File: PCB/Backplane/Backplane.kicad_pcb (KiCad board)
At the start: 4 copper layers, 40 x 100 mm, 79 parts, among them J1 ICSP, J2 Front, J3 Rear, J4 Bus In, J5 Bus Out, J6 Power In, J7 Power Out, Q1 Q_NMOS_GSD, Q2 Q_NMOS_GSD, SW1 Boot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

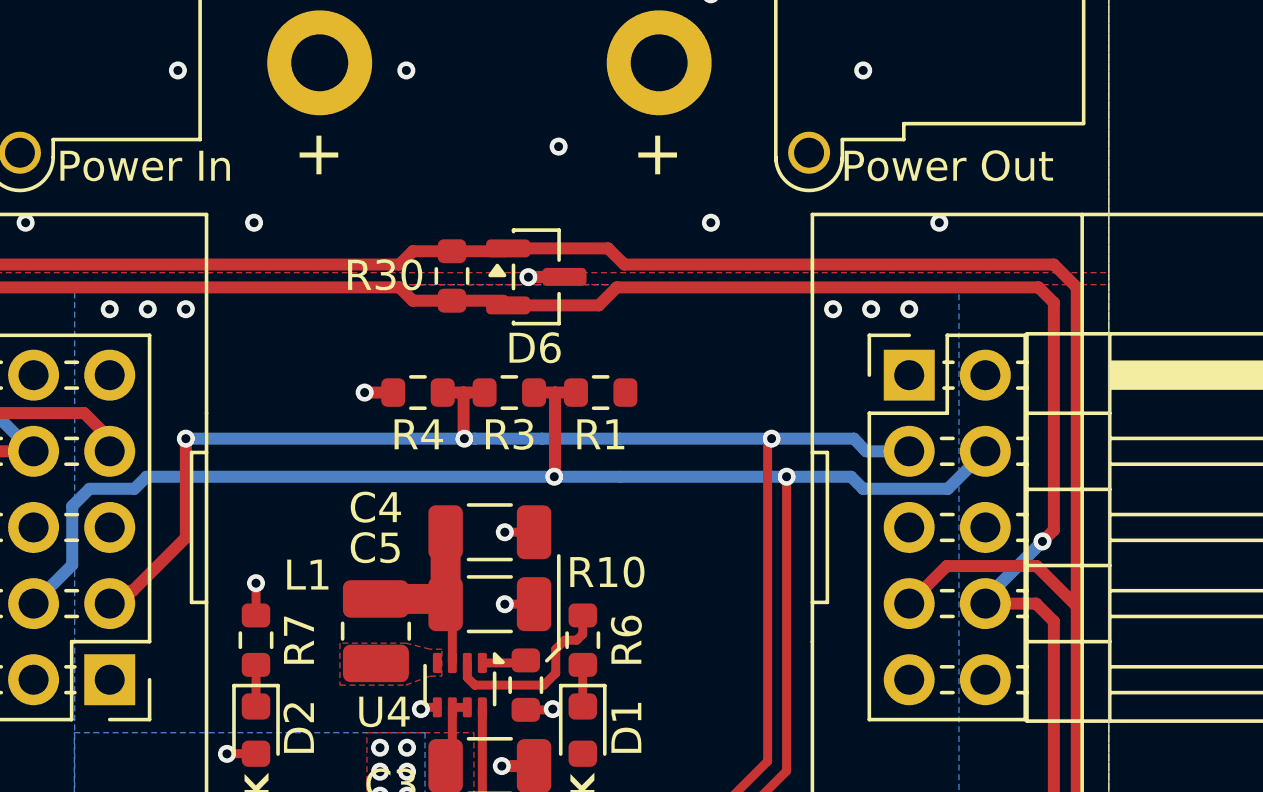
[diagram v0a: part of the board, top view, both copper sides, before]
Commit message: Add ESD protection to the RS485 networks.
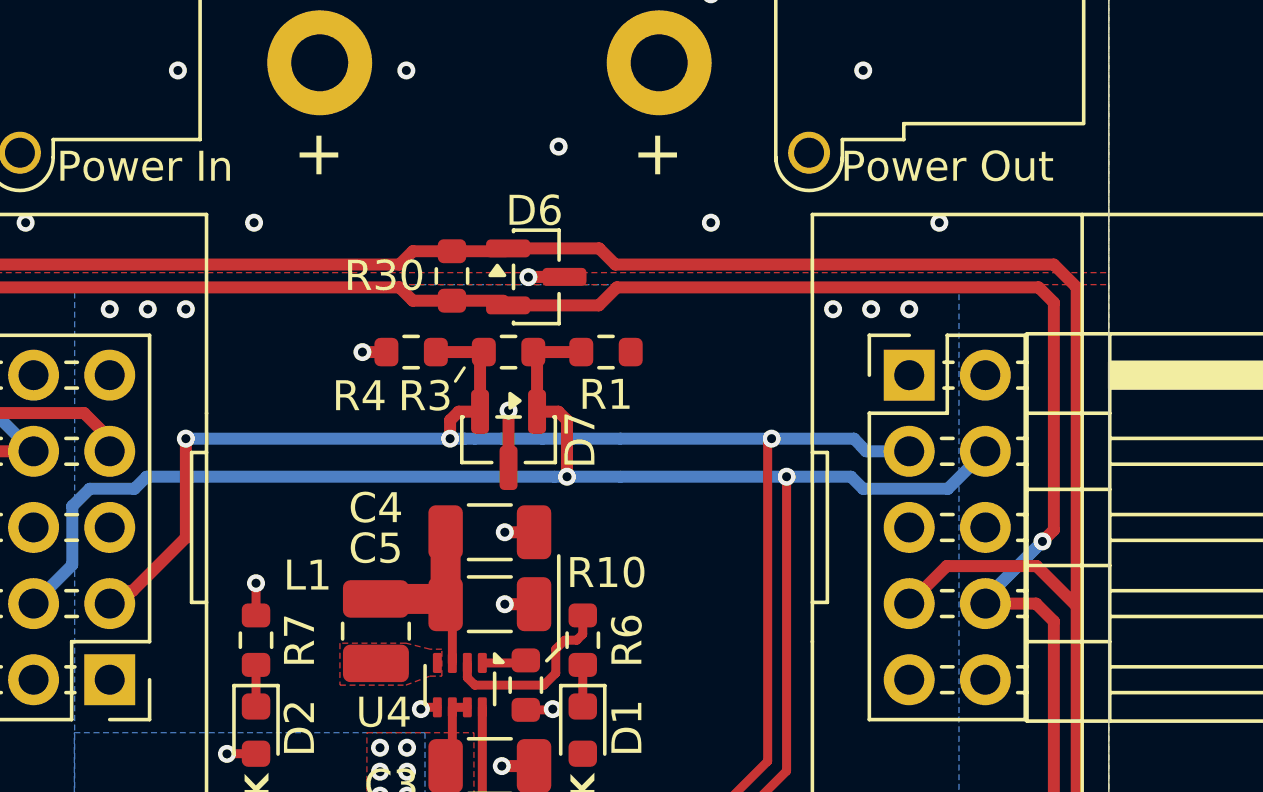
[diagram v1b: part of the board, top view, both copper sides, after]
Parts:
- added D7: T24CAN, Package_TO_SOT_SMD:SOT-23, F.Cu at (40.0, 50.1)
- moved R4 1.37 mm to (36.7, 47.1)
- moved R1 1.36 mm to (43.2, 47.1)
- moved R3 1.35 mm to (40.0, 47.1)
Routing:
- net A: track 60.9 -> 63.3 mm
- net B: track 56.2 -> 58.6 mm
- net GND: track 63.8 -> 65.6 mm, vias 51 -> 52

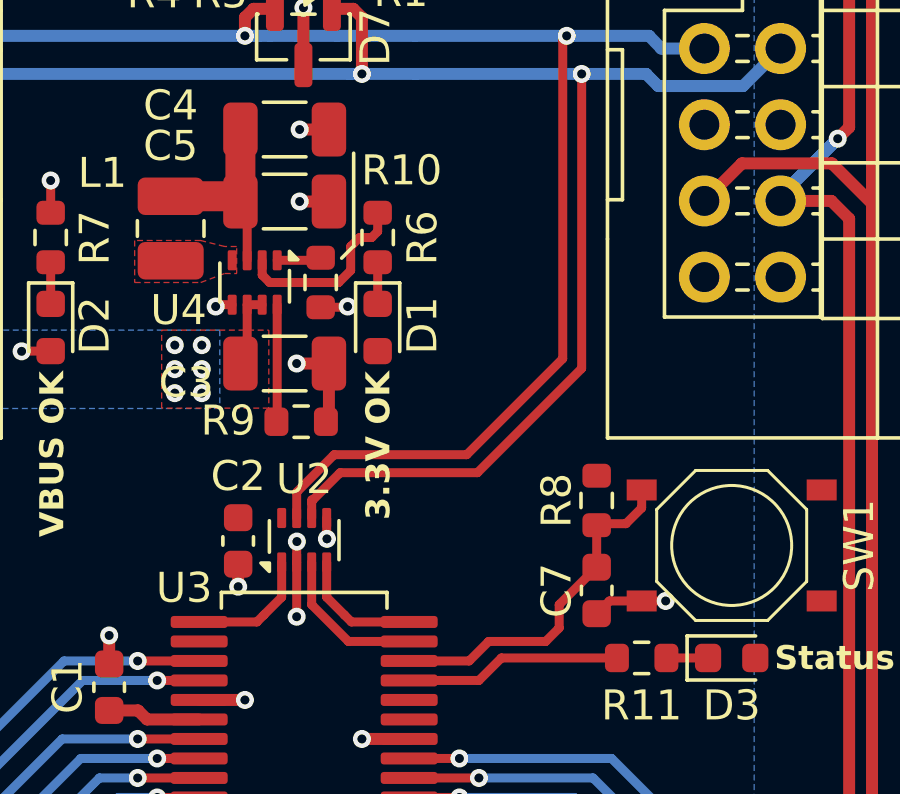
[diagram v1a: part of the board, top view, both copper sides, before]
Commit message: Fix up power LEDs on regulators.
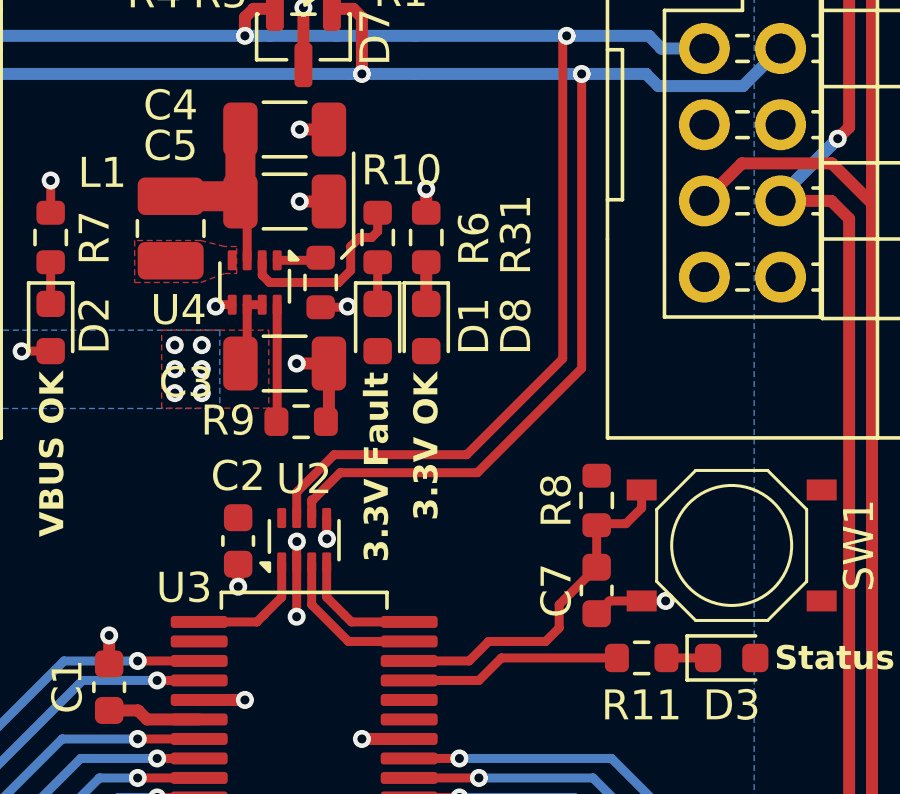
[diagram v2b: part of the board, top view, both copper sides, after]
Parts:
- added D8: 3.3V OK, LED_SMD:LED_0603_1608Metric, F.Cu at (44.1, 59.8)
- added R31: 10k, Resistor_SMD:R_0603_1608Metric, F.Cu at (44.1, 56.8)
- D1: value 3.3V OK -> 3.3V Fault
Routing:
- net Net-(D8-K): track 0.00 -> 1.39 mm
- net GND: track 65.6 -> 66.4 mm, vias 52 -> 53
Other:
- board text added: "3.3V Fault"

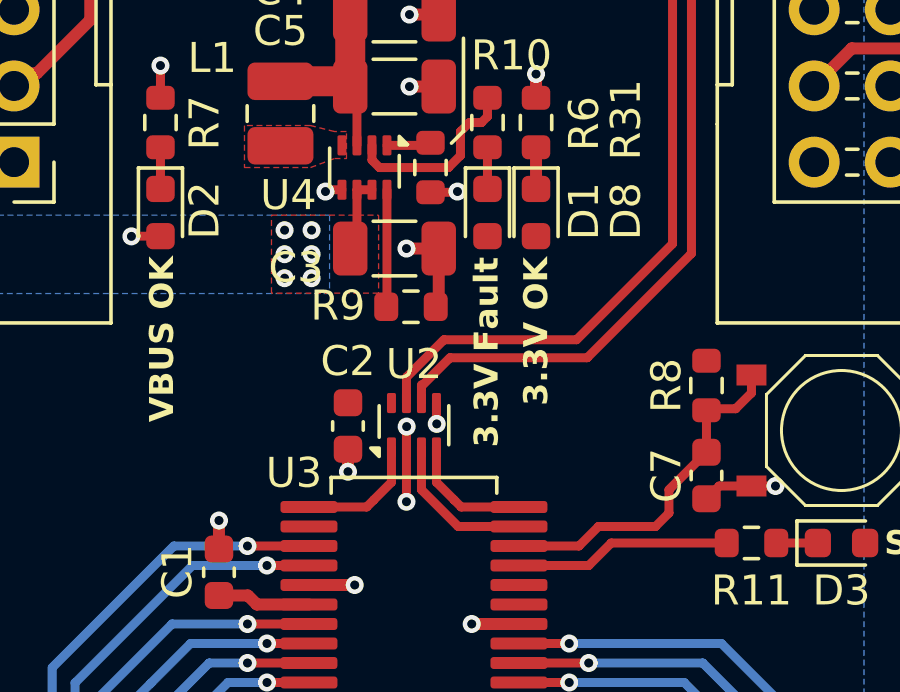
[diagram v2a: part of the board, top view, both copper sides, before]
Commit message: Include all corrections, mint new gerbers. Update some to KiCad 10.
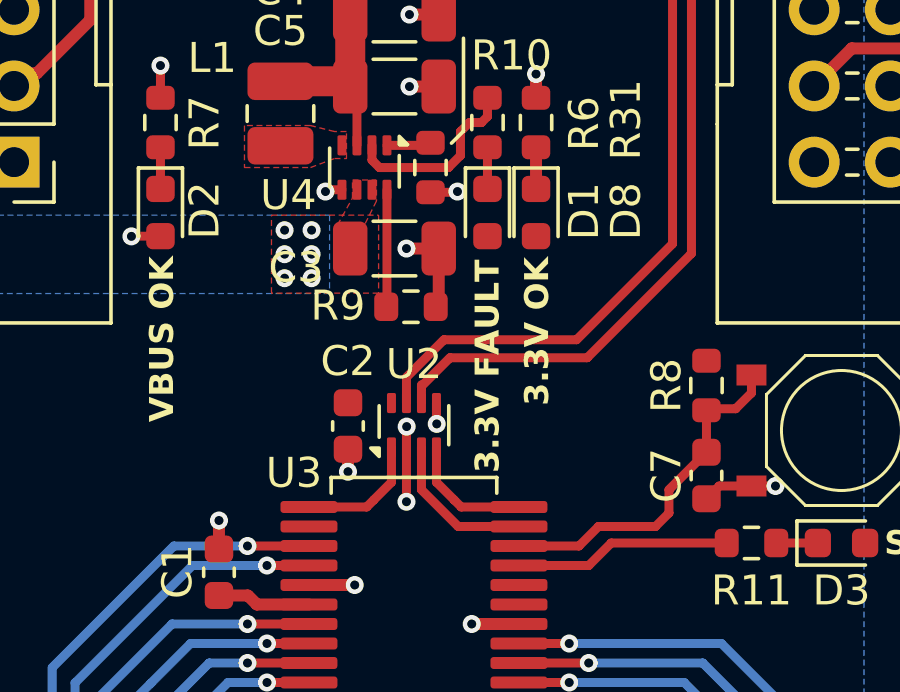
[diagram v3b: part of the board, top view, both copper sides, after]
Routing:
- net VDD: track 4.40 -> 2.16 mm
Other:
- board text added: "3.3V FAULT"
- board text removed: "3.3V Fault"

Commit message: feat: Upgrade backplane to a STM32G070KB.
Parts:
- removed U3: PIC18F25Q43, Package_SO:SSOP-28_5.3x10.2mm_P0.65mm
- added C25: 4.7uF, Capacitor_SMD:C_0603_1608Metric, F.Cu at (46.6, 76.7)
- added U11: STM32G070KBTx, Package_QFP:LQFP-32_7x7mm_P0.8mm, F.Cu at (40.0, 75.5)
- H1, H2, H3, H4: footprint MountingHole:MountingHole_3.2mm_M3 -> KTANE:MountingHole_3.2mm_M3_NoCopper
- J1: value ICSP -> SWD
- R31: value 10k -> 1000
- R6: value 1000 -> 10k
- moved C1 15.5 mm to (48.1, 76.7), turned to -90 degrees
- moved C6 7.25 mm to (48.1, 73.6), turned to 90 degrees
- moved R5 7.25 mm to (46.6, 73.6), turned to -90 degrees
- moved J1 2.97 mm to (40.0, 84.5), turned to 0 degrees
- moved R15 0.81 mm to (31.7, 84.0)
- moved D4 0.81 mm to (34.7, 84.0)
- moved G*** 0.75 mm to (23.1, 79.9)
- moved D5 0.25 mm to (45.2, 84.0)
- moved R23 0.25 mm to (48.2, 84.0)
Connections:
- net Net-(U5-ILM) renamed FRONT-ILM
- net Net-(U7-ILM) renamed REAR-ILM
- C6 pad 1: ~{MCLR} -> ~{RESET}
- D1 pad 2: +3.3V -> VDD
- J1 pad 1: ~{MCLR} -> +3.3V
- J1 pad 2: +3.3V -> SWDIO
- J1 pad 3: GND -> ~{RESET}
- J1 pad 4: ICSPDAT -> SWCLK
- J1 pad 5: ICSPCLK -> GND
- R5 pad 2: ~{MCLR} -> ~{RESET}
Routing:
- net FRONT-ILM: track 2.12 -> 47.4 mm, vias 0 -> 2
- net ~{RESET}: track 0.00 -> 20.2 mm, vias 0 -> 2
- net REAR-ILM: track 2.12 -> 21.4 mm, vias 0 -> 2
- net ICSPDAT: track 8.09 -> 0.00 mm, vias 2 -> 0
- net ~{MCLR}: track 7.55 -> 0.00 mm
- net VDD: track 2.16 -> 9.66 mm, vias 35 -> 36
- net SWDIO: track 0.00 -> 6.77 mm
- net STATUS-LED: track 7.24 -> 12.7 mm, vias 0 -> 2
- net SWCLK: track 0.00 -> 5.35 mm
- net ICSPCLK: track 5.30 -> 0.00 mm
- net REAR-BOOT: track 27.4 -> 30.6 mm
- net BOOT: track 11.7 -> 14.8 mm
- net FRONT-MODULE-DETECT: track 31.1 -> 28.3 mm
- net FRONT-UART-TX: track 35.7 -> 33.0 mm
- net FRONT-EFUSE-FLT: track 44.7 -> 42.0 mm
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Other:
- board text added: "KTANE IRL by Melair Backplane (B01)"
- board text removed: "+"
- board text removed: "-"
- board text removed: "KTANE IRL by Melair Backplane (A02)"
